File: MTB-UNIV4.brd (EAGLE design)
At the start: 100 x 80 mm, 27 parts, among them IC1 MEGA128-A, IC2 SN75176AP, IC3 NCP1117, X1 MKDSN1,5/4-5,08, X2 MKDSN1,5/4-5,08

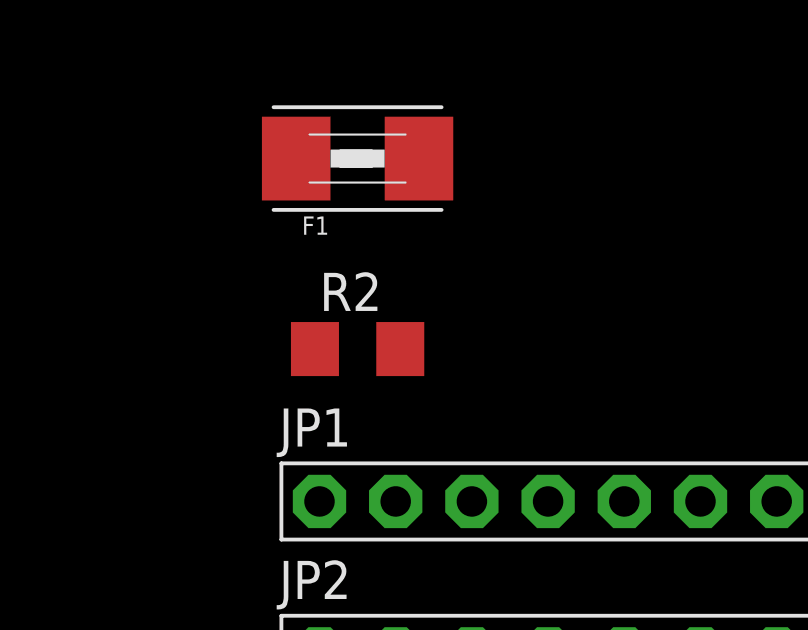
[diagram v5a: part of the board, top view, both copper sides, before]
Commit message: odstraněn odpor zátěže pro RS-485. dle požadavku v #4
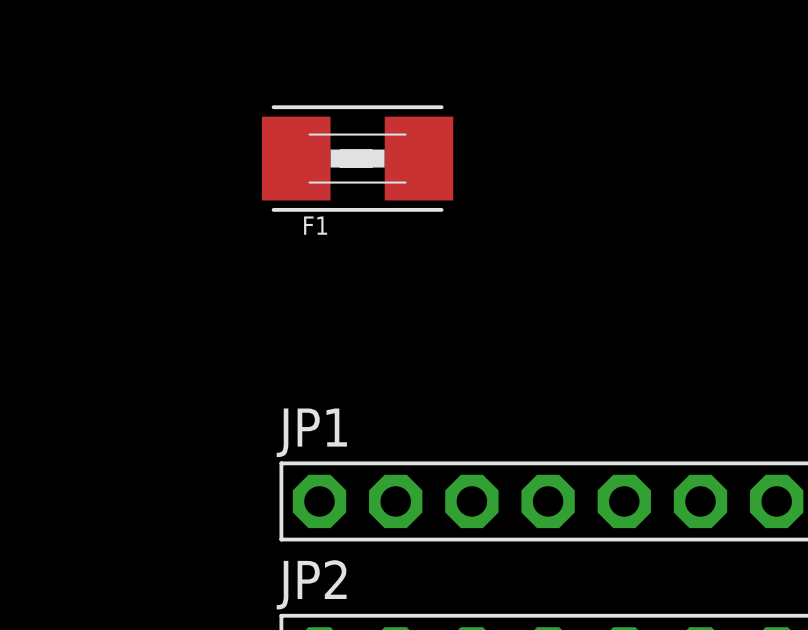
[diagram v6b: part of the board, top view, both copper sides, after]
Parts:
- removed R2: (no value), rcl:R1206
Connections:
- net RS-A: no longer R2.1
- net RS-B: no longer R2.2
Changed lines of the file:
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@@
 <attribute name="VALUE" x="-69.1675" y="-161.925" size="0.6096" layer="27"/>
-</element>
-<element name="R2" library="rcl" library_urn="urn:adsk.eagle:library:334" package="R1206" package3d_urn="urn:adsk.eagle:package:23540/2" value="" x="-67.31" y="-170.18" smashed="yes">
-<attribute name="NAME" x="-68.58" y="-168.91" size="1.27" layer="25"/>
-<attribute name="POPULARITY" value="41" x="-67.31" y="-170.18" size="1.778" layer="27" display="off"/>
-<attribute name="SPICEPREFIX" value="R" x="-67.31" y="-170.18" size="1.778" layer="27" display="off"/>
-<attribute name="VALUE" x="-68.58" y="-172.72" size="1.27" layer="27"/>
 </element>
 <element name="JP1" library="adafruit" library_urn="urn:adsk.eagle:library:420" package="1X08-BIG" package3d_urn="urn:adsk.eagle:package:6240707/1" value="" x="-59.69" y="-175.26" smashed="yes">
@@
 <contactref element="IC2" pad="6"/>
 <contactref element="X2" pad="2"/>
-<contactref element="R2" pad="1"/>
 <contactref element="X1" pad="2"/>
-<wire x1="-26.6911" y1="-79.985" x2="-68.732" y2="-170.18" width="0" layer="19" extent="1-1"/>
 <wire x1="-26.6911" y1="-68.555" x2="-26.6911" y2="-79.985" width="0" layer="19" extent="1-1"/>
 <wire x1="-19.05" y1="-52.07" x2="-26.6911" y2="-68.555" width="0" layer="19" extent="1-1"/>
@@
 <signal name="RS-B">
 <contactref element="IC2" pad="7"/>
-<contactref element="R2" pad="2"/>
 <contactref element="X1" pad="3"/>
 <contactref element="X2" pad="3"/>
-<wire x1="-21.6111" y1="-79.985" x2="-65.888" y2="-170.18" width="0" layer="19" extent="1-1"/>
 <wire x1="-21.6111" y1="-68.555" x2="-21.6111" y2="-79.985" width="0" layer="19" extent="1-1"/>
 <wire x1="-21.59" y1="-52.07" x2="-21.6111" y2="-68.555" width="0" layer="19" extent="1-1"/>

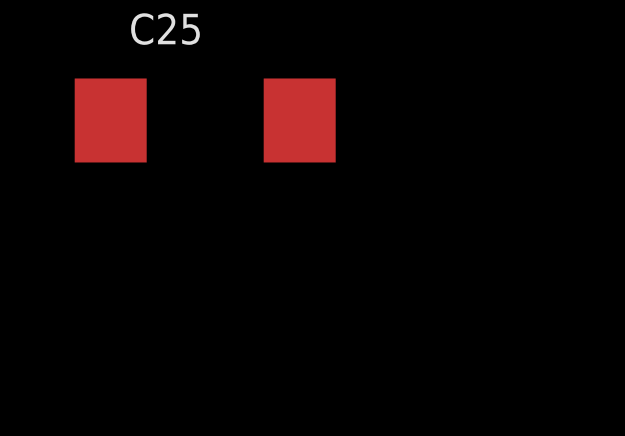
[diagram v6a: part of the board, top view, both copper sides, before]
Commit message: přidán svodový kondenzátor C27 pro MCU (vývody na více stranách. řešení pro #3
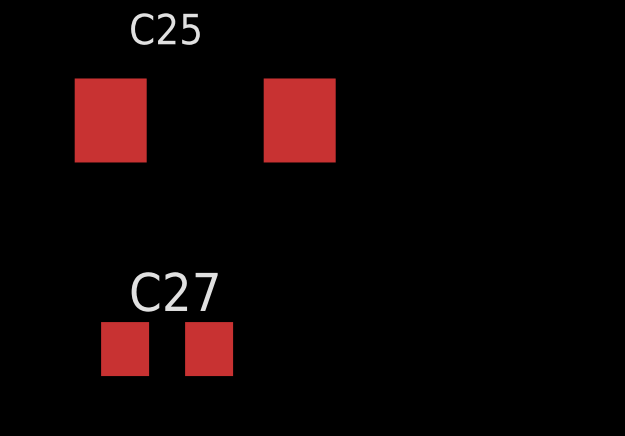
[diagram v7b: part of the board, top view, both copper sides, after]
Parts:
- added C27: 100nF, rcl:C1206
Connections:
- net +5V: now also C27.1
- net GND: now also C27.2
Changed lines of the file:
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@@
 <attribute name="VALUE" x="-74.93" y="-195.58" size="1.016" layer="27"/>
+</element>
+<element name="C27" library="rcl" library_urn="urn:adsk.eagle:library:334" package="C1206" package3d_urn="urn:adsk.eagle:package:23618/2" value="100nF" x="-73.66" y="-199.39" smashed="yes">
+<attribute name="NAME" x="-74.93" y="-198.12" size="1.27" layer="25"/>
+<attribute name="POPULARITY" value="54" x="-73.66" y="-199.39" size="1.778" layer="27" display="off"/>
+<attribute name="SPICEPREFIX" value="C" x="-73.66" y="-199.39" size="1.778" layer="27" display="off"/>
+<attribute name="VALUE" x="-74.93" y="-201.93" size="1.27" layer="27"/>
 </element>
 </elements>
@@
 <contactref element="C25" pad="-"/>
 <contactref element="C26" pad="-"/>
+<contactref element="C27" pad="2"/>
 <wire x1="-65.91" y1="-120.65" x2="-65.91" y2="-125.73" width="0" layer="19" extent="1-1"/>
 <wire x1="-69.61" y1="-114.91" x2="-65.91" y2="-120.65" width="0" layer="19" extent="1-1"/>
@@
 <wire x1="-68.58" y1="-185.42" x2="-73.43" y2="-184.15" width="0" layer="19" extent="1-1"/>
 <wire x1="-69.24" y1="-191.77" x2="-68.58" y2="-185.42" width="0" layer="19" extent="1-1"/>
+<wire x1="-72.26" y1="-199.39" x2="-69.24" y2="-191.77" width="0" layer="19" extent="1-1"/>
 </signal>
 <signal name="+5V">
@@
 <contactref element="C3" pad="1"/>
 <contactref element="C26" pad="+"/>
+<contactref element="C27" pad="1"/>
 <wire x1="-67.31" y1="-114.91" x2="-68.71" y2="-125.73" width="0" layer="19" extent="1-1"/>
 <wire x1="-67.31" y1="-108.61" x2="-67.31" y2="-114.91" width="0" layer="19" extent="1-1"/>
@@
 <wire x1="-15.45" y1="-13.79" x2="-25.05" y2="-13.79" width="0" layer="19" extent="1-1"/>
 <wire x1="-76.43" y1="-184.15" x2="-68.71" y2="-125.73" width="0" layer="19" extent="1-1"/>
+<wire x1="-75.06" y1="-199.39" x2="-76.43" y2="-184.15" width="0" layer="19" extent="1-1"/>
 </signal>
 <signal name="MISO">

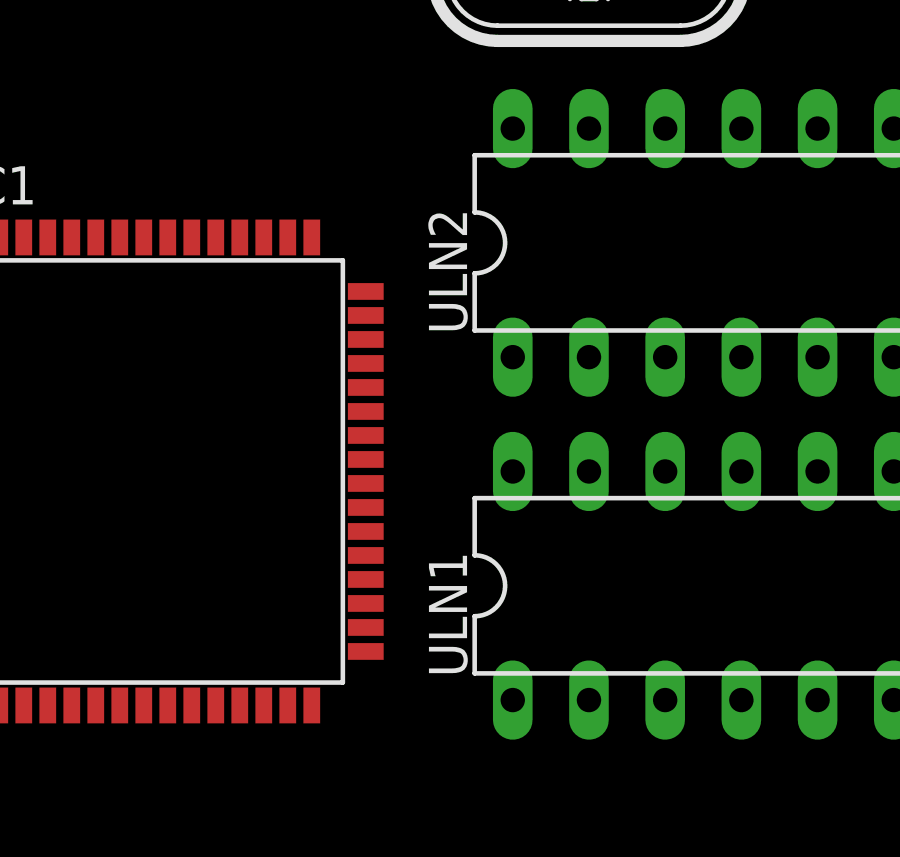
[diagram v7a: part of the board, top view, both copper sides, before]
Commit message: přejmenovány ULN
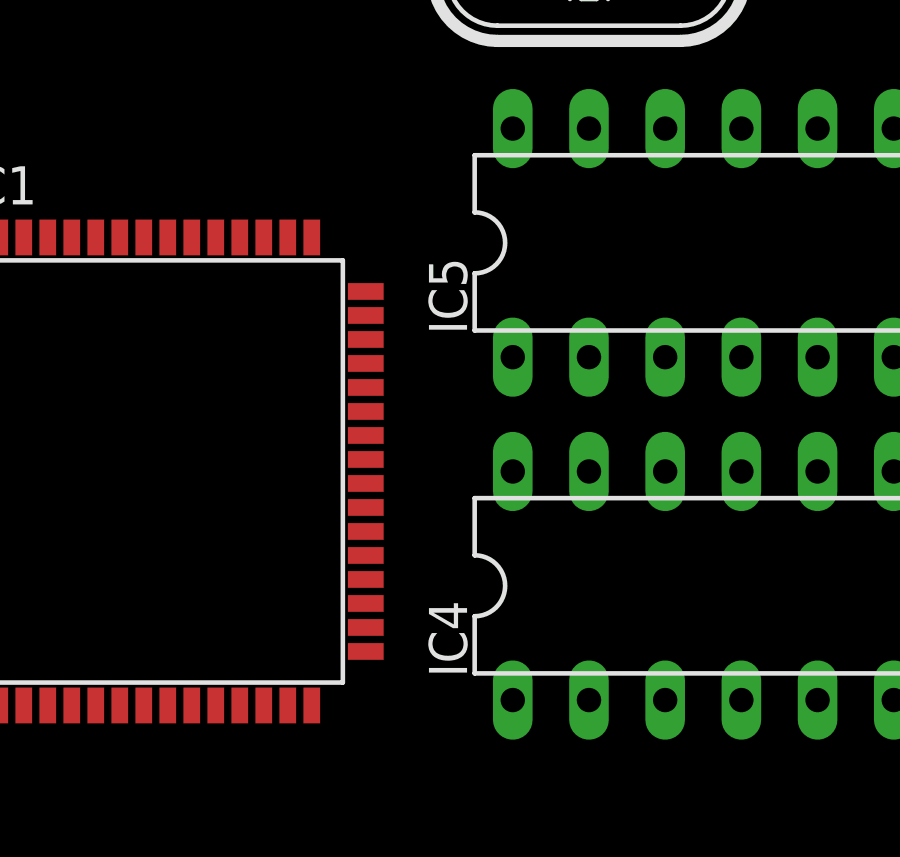
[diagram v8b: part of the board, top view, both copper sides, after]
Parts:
- renumbered ULN1 to IC4, ULN2 to IC5
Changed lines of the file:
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@@
 <attribute name="VALUE" x="-8.89" y="-9.017" size="1.27" layer="27" ratio="10"/>
 </element>
-<element name="ULN2" library="uln-udn" library_urn="urn:adsk.eagle:library:407" package="DIL18" package3d_urn="urn:adsk.eagle:package:16424/2" value="ULN2803A" x="3.81" y="-13.97" smashed="yes">
+<element name="IC5" library="uln-udn" library_urn="urn:adsk.eagle:library:407" package="DIL18" package3d_urn="urn:adsk.eagle:package:16424/2" value="ULN2803A" x="3.81" y="-13.97" smashed="yes">
 <attribute name="NAME" x="-7.874" y="-17.018" size="1.27" layer="25" ratio="10" rot="R90"/>
 <attribute name="POPULARITY" value="5" x="3.81" y="-13.97" size="1.778" layer="27" display="off"/>
 <attribute name="VALUE" x="-5.715" y="-14.605" size="1.27" layer="27" ratio="10"/>
 </element>
-<element name="ULN1" library="uln-udn" library_urn="urn:adsk.eagle:library:407" package="DIL18" package3d_urn="urn:adsk.eagle:package:16424/2" value="ULN2803A" x="3.81" y="-25.4" smashed="yes">
+<element name="IC4" library="uln-udn" library_urn="urn:adsk.eagle:library:407" package="DIL18" package3d_urn="urn:adsk.eagle:package:16424/2" value="ULN2803A" x="3.81" y="-25.4" smashed="yes">
 <attribute name="NAME" x="-7.874" y="-28.448" size="1.27" layer="25" ratio="10" rot="R90"/>
 <attribute name="POPULARITY" value="5" x="3.81" y="-25.4" size="1.778" layer="27" display="off"/>
@@
 <signals>
 <signal name="GND">
-<contactref element="ULN1" pad="9"/>
-<contactref element="ULN1" pad="10"/>
-<contactref element="ULN2" pad="9"/>
-<contactref element="ULN2" pad="10"/>
+<contactref element="IC4" pad="9"/>
+<contactref element="IC4" pad="10"/>
+<contactref element="IC5" pad="9"/>
+<contactref element="IC5" pad="10"/>
 <contactref element="IC1" pad="63"/>
 <contactref element="IC1" pad="53"/>
@@
 <signal name="D-OUT(A)1">
 <contactref element="IC1" pad="25"/>
-<contactref element="ULN1" pad="1"/>
+<contactref element="IC4" pad="1"/>
 <wire x1="-6.35" y1="-29.21" x2="-18.65" y2="-29.39" width="0" layer="19" extent="1-1"/>
 </signal>
 <signal name="D-OUT(A)2">
 <contactref element="IC1" pad="26"/>
-<contactref element="ULN1" pad="2"/>
+<contactref element="IC4" pad="2"/>
 <wire x1="-3.81" y1="-29.21" x2="-17.85" y2="-29.39" width="0" layer="19" extent="1-1"/>
 </signal>
 <signal name="D-OUT(A)3">
 <contactref element="IC1" pad="27"/>
-<contactref element="ULN1" pad="3"/>
+<contactref element="IC4" pad="3"/>
 <wire x1="-1.27" y1="-29.21" x2="-17.05" y2="-29.39" width="0" layer="19" extent="1-1"/>
 </signal>
 <signal name="D-OUT(A)4">
 <contactref element="IC1" pad="28"/>
-<contactref element="ULN1" pad="4"/>
+<contactref element="IC4" pad="4"/>
 <wire x1="1.27" y1="-29.21" x2="-16.25" y2="-29.39" width="0" layer="19" extent="1-1"/>
 </signal>
 <signal name="D-OUT(A)5">
 <contactref element="IC1" pad="29"/>
-<contactref element="ULN1" pad="5"/>
+<contactref element="IC4" pad="5"/>
 <wire x1="3.81" y1="-29.21" x2="-15.45" y2="-29.39" width="0" layer="19" extent="1-1"/>
 </signal>
 <signal name="D-OUT(A)6">
 <contactref element="IC1" pad="30"/>
-<contactref element="ULN1" pad="6"/>
+<contactref element="IC4" pad="6"/>
 <wire x1="6.35" y1="-29.21" x2="-14.65" y2="-29.39" width="0" layer="19" extent="1-1"/>
 </signal>
 <signal name="D-OUT(A)7">
 <contactref element="IC1" pad="31"/>
-<contactref element="ULN1" pad="7"/>
+<contactref element="IC4" pad="7"/>
 <wire x1="8.89" y1="-29.21" x2="-13.85" y2="-29.39" width="0" layer="19" extent="1-1"/>
 </signal>
 <signal name="D-OUT(A)8">
 <contactref element="IC1" pad="32"/>
-<contactref element="ULN1" pad="8"/>
+<contactref element="IC4" pad="8"/>
 <wire x1="11.43" y1="-29.21" x2="-13.05" y2="-29.39" width="0" layer="19" extent="1-1"/>
 </signal>
 <signal name="D-OUT(B)1">
 <contactref element="IC1" pad="61"/>
-<contactref element="ULN2" pad="1"/>
+<contactref element="IC5" pad="1"/>
 <wire x1="-6.35" y1="-17.78" x2="-22.65" y2="-13.79" width="0" layer="19" extent="1-1"/>
 </signal>
 <signal name="D-OUT(B)2">
 <contactref element="IC1" pad="60"/>
-<contactref element="ULN2" pad="2"/>
+<contactref element="IC5" pad="2"/>
 <wire x1="-3.81" y1="-17.78" x2="-21.85" y2="-13.79" width="0" layer="19" extent="1-1"/>
 </signal>
 <signal name="D-OUT(B)3">
 <contactref element="IC1" pad="59"/>
-<contactref element="ULN2" pad="3"/>
+<contactref element="IC5" pad="3"/>
 <wire x1="-1.27" y1="-17.78" x2="-21.05" y2="-13.79" width="0" layer="19" extent="1-1"/>
 </signal>
 <signal name="D-OUT(B)4">
 <contactref element="IC1" pad="58"/>
-<contactref element="ULN2" pad="4"/>
+<contactref element="IC5" pad="4"/>
 <wire x1="1.27" y1="-17.78" x2="-20.25" y2="-13.79" width="0" layer="19" extent="1-1"/>
 </signal>
 <signal name="D-OUT(B)5">
 <contactref element="IC1" pad="57"/>
-<contactref element="ULN2" pad="5"/>
+<contactref element="IC5" pad="5"/>
 <wire x1="3.81" y1="-17.78" x2="-19.45" y2="-13.79" width="0" layer="19" extent="1-1"/>
 </signal>
 <signal name="D-OUT(B)6">
 <contactref element="IC1" pad="56"/>
-<contactref element="ULN2" pad="6"/>
+<contactref element="IC5" pad="6"/>
 <wire x1="6.35" y1="-17.78" x2="-18.65" y2="-13.79" width="0" layer="19" extent="1-1"/>
 </signal>
 <signal name="D-OUT(B)7">
 <contactref element="IC1" pad="55"/>
-<contactref element="ULN2" pad="7"/>
+<contactref element="IC5" pad="7"/>
 <wire x1="8.89" y1="-17.78" x2="-17.85" y2="-13.79" width="0" layer="19" extent="1-1"/>
 </signal>
 <signal name="D-OUT(B)8">
 <contactref element="IC1" pad="54"/>
-<contactref element="ULN2" pad="8"/>
+<contactref element="IC5" pad="8"/>
 <wire x1="11.43" y1="-17.78" x2="-17.05" y2="-13.79" width="0" layer="19" extent="1-1"/>
 </signal>
 <signal name="N$2">
-<contactref element="ULN1" pad="11"/>
+<contactref element="IC4" pad="11"/>
 <contactref element="JP1" pad="8"/>
 <wire x1="11.43" y1="-21.59" x2="-50.8" y2="-175.26" width="0" layer="19" extent="1-1"/>
 </signal>
 <signal name="N$4">
-<contactref element="ULN1" pad="12"/>
+<contactref element="IC4" pad="12"/>
 <contactref element="JP1" pad="7"/>
 <wire x1="8.89" y1="-21.59" x2="-53.34" y2="-175.26" width="0" layer="19" extent="1-1"/>
 </signal>
 <signal name="N$5">
-<contactref element="ULN1" pad="13"/>
+<contactref element="IC4" pad="13"/>
 <contactref element="JP1" pad="6"/>
 <wire x1="6.35" y1="-21.59" x2="-55.88" y2="-175.26" width="0" layer="19" extent="1-1"/>
 </signal>
 <signal name="N$6">
-<contactref element="ULN1" pad="14"/>
+<contactref element="IC4" pad="14"/>
 <contactref element="JP1" pad="5"/>
 <wire x1="3.81" y1="-21.59" x2="-58.42" y2="-175.26" width="0" layer="19" extent="1-1"/>
 </signal>
 <signal name="N$7">
-<contactref element="ULN1" pad="15"/>
+<contactref element="IC4" pad="15"/>
 <contactref element="JP1" pad="4"/>
 <wire x1="1.27" y1="-21.59" x2="-60.96" y2="-175.26" width="0" layer="19" extent="1-1"/>
 </signal>
 <signal name="N$8">
-<contactref element="ULN1" pad="16"/>
+<contactref element="IC4" pad="16"/>
 <contactref element="JP1" pad="3"/>
 <wire x1="-1.27" y1="-21.59" x2="-63.5" y2="-175.26" width="0" layer="19" extent="1-1"/>
 </signal>
 <signal name="N$9">
-<contactref element="ULN1" pad="17"/>
+<contactref element="IC4" pad="17"/>
 <contactref element="JP1" pad="2"/>
 <wire x1="-3.81" y1="-21.59" x2="-66.04" y2="-175.26" width="0" layer="19" extent="1-1"/>
 </signal>
 <signal name="N$10">
-<contactref element="ULN1" pad="18"/>
+<contactref element="IC4" pad="18"/>
 <contactref element="JP1" pad="1"/>
 <wire x1="-6.35" y1="-21.59" x2="-68.58" y2="-175.26" width="0" layer="19" extent="1-1"/>
 </signal>
 <signal name="N$11">
-<contactref element="ULN2" pad="11"/>
+<contactref element="IC5" pad="11"/>
 <contactref element="JP2" pad="8"/>
 <wire x1="11.43" y1="-10.16" x2="-50.8" y2="-180.34" width="0" layer="19" extent="1-1"/>
 </signal>
 <signal name="N$12">
-<contactref element="ULN2" pad="12"/>
+<contactref element="IC5" pad="12"/>
 <contactref element="JP2" pad="7"/>
 <wire x1="8.89" y1="-10.16" x2="-53.34" y2="-180.34" width="0" layer="19" extent="1-1"/>
 </signal>
 <signal name="N$15">
-<contactref element="ULN2" pad="13"/>
+<contactref element="IC5" pad="13"/>
 <contactref element="JP2" pad="6"/>
 <wire x1="6.35" y1="-10.16" x2="-55.88" y2="-180.34" width="0" layer="19" extent="1-1"/>
 </signal>
 <signal name="N$16">
-<contactref element="ULN2" pad="14"/>
+<contactref element="IC5" pad="14"/>
 <contactref element="JP2" pad="5"/>
 <wire x1="3.81" y1="-10.16" x2="-58.42" y2="-180.34" width="0" layer="19" extent="1-1"/>
 </signal>
 <signal name="N$17">
-<contactref element="ULN2" pad="15"/>
+<contactref element="IC5" pad="15"/>
 <contactref element="JP2" pad="4"/>
 <wire x1="1.27" y1="-10.16" x2="-60.96" y2="-180.34" width="0" layer="19" extent="1-1"/>
 </signal>
 <signal name="N$18">
-<contactref element="ULN2" pad="16"/>
+<contactref element="IC5" pad="16"/>
 <contactref element="JP2" pad="3"/>
 <wire x1="-1.27" y1="-10.16" x2="-63.5" y2="-180.34" width="0" layer="19" extent="1-1"/>
 </signal>
 <signal name="N$19">
-<contactref element="ULN2" pad="17"/>
+<contactref element="IC5" pad="17"/>
 <contactref element="JP2" pad="2"/>
 <wire x1="-3.81" y1="-10.16" x2="-66.04" y2="-180.34" width="0" layer="19" extent="1-1"/>
 </signal>
 <signal name="N$20">
-<contactref element="ULN2" pad="18"/>
+<contactref element="IC5" pad="18"/>
 <contactref element="JP2" pad="1"/>
 <wire x1="-6.35" y1="-10.16" x2="-68.58" y2="-180.34" width="0" layer="19" extent="1-1"/>
